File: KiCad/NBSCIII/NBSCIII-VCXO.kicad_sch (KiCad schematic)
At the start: 20 parts, among them Q1000 BC337-25, Q1001 2SC1906, X1000 6.000Mhz HC49/U

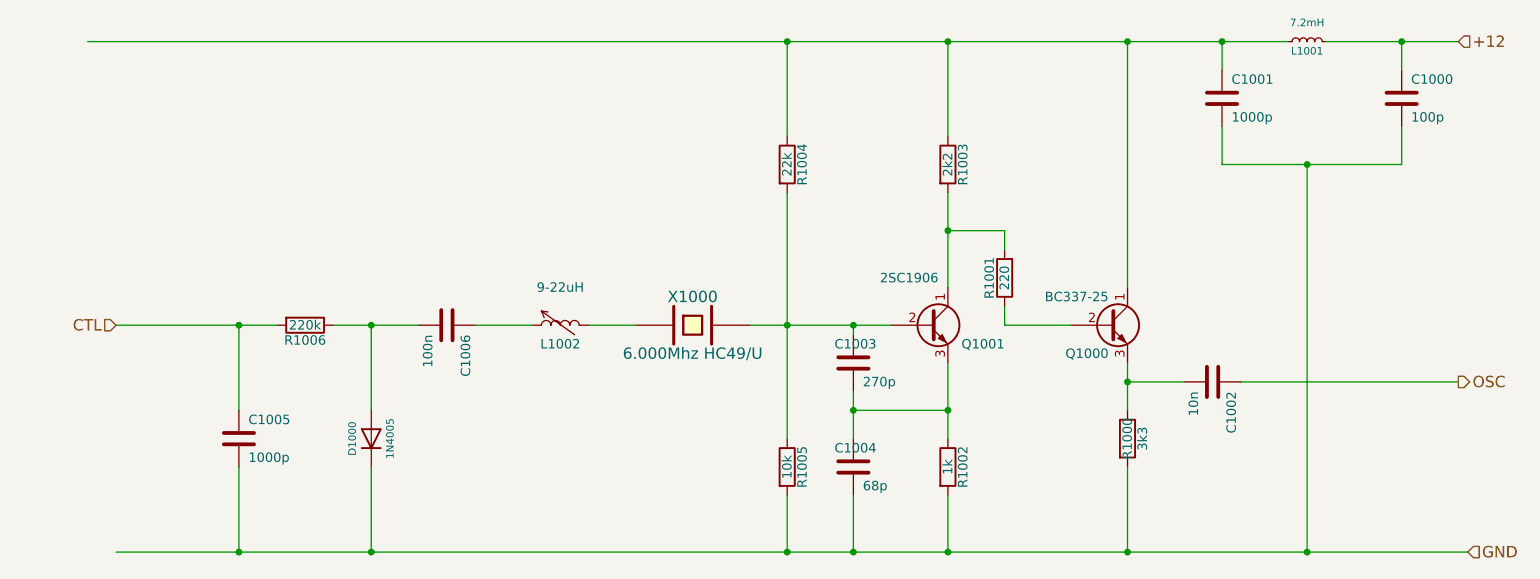
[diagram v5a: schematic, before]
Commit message: Simplify power distribution and make global
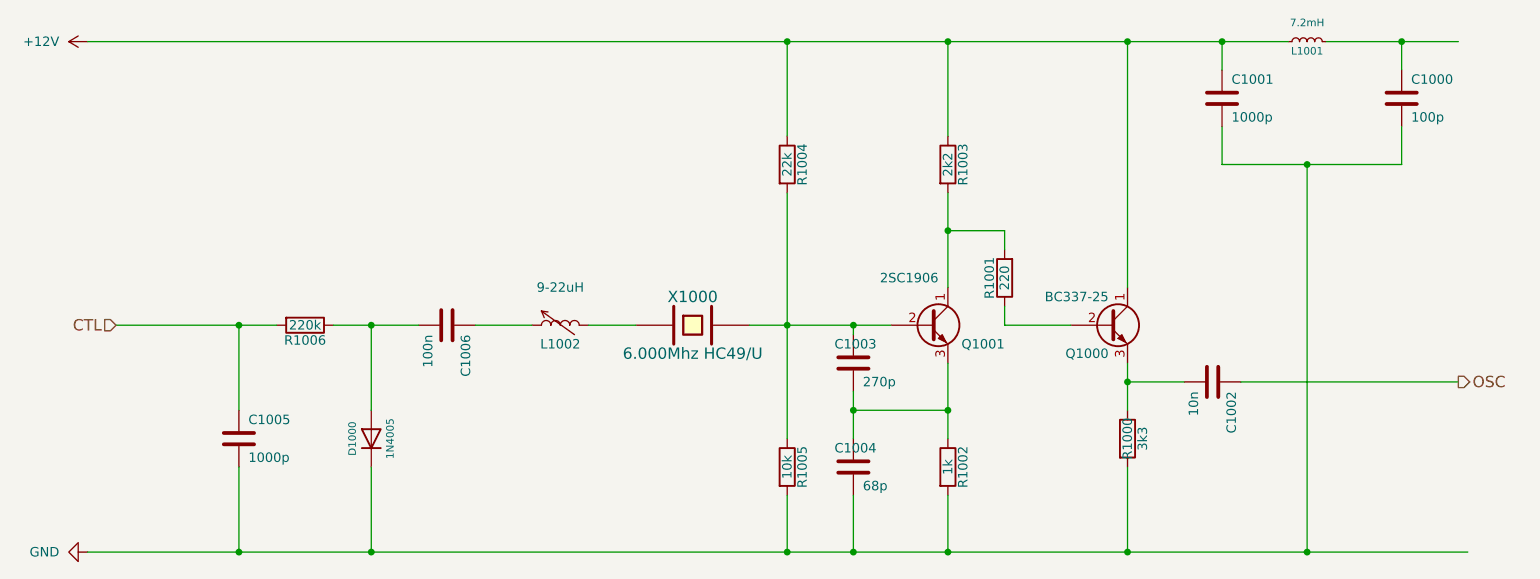
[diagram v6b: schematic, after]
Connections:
- net +12V: now reaches C1001.1, L1001.1, Q1000.1 (C), R1003.1, R1004.1
- net +12: no longer names the net of C1000.1, L1001.2
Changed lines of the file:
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@@
     (stroke (width 0) (type default) (color 0 0 0 0))
   )
-  (wire (pts (xy 46.99 123.19) (xy 63.5 123.19))
+  (wire (pts (xy 43.18 123.19) (xy 63.5 123.19))
     (stroke (width 0) (type default) (color 0 0 0 0))
   )
@@
   (wire (pts (xy 198.12 100.33) (xy 227.33 100.33))
     (stroke (width 0) (type default) (color 0 0 0 0))
-  )
-  (hierarchical_label "GND" (shape input) (at 228.6 123.19 0)
-    (effects (font (size 1.524 1.524)) (justify left))
   )
   (hierarchical_label "CTL" (shape input) (at 46.99 92.71 180)
@@
   )
   (hierarchical_label "OSC" (shape output) (at 227.33 100.33 0)
-    (effects (font (size 1.524 1.524)) (justify left))
-  )
-  (hierarchical_label "+12" (shape input) (at 227.33 54.61 0)
     (effects (font (size 1.524 1.524)) (justify left))
   )
@@
     (pin "2")
   )
+  (symbol (lib_id "power:GND") (at 43.18 123.19 270) (unit 1)
+    (in_bom yes) (on_board yes) (fields_autoplaced)
+    (property "Reference" "#PWR0129" (id 0) (at 36.83 123.19 0)
+      (effects (font (size 1.27 1.27)) hide)
+    )
+    (property "Value" "GND" (id 1) (at 39.37 123.1899 90)
+      (effects (font (size 1.27 1.27)) (justify right))
+    )
+    (property "Footprint" "" (id 2) (at 43.18 123.19 0)
+      (effects (font (size 1.27 1.27)) hide)
+    )
+    (property "Datasheet" "" (id 3) (at 43.18 123.19 0)
+      (effects (font (size 1.27 1.27)) hide)
+    )
+    (pin "1")
+  )
+  (symbol (lib_id "power:+12V") (at 43.18 54.61 90) (unit 1)
+    (in_bom yes) (on_board yes) (fields_autoplaced)
+    (property "Reference" "#PWR0128" (id 0) (at 46.99 54.61 0)
+      (effects (font (size 1.27 1.27)) hide)
+    )
+    (property "Value" "+12V" (id 1) (at 39.37 54.6099 90)
+      (effects (font (size 1.27 1.27)) (justify left))
+    )
+    (property "Footprint" "" (id 2) (at 43.18 54.61 0)
+      (effects (font (size 1.27 1.27)) hide)
+    )
+    (property "Datasheet" "" (id 3) (at 43.18 54.61 0)
+      (effects (font (size 1.27 1.27)) hide)
+    )
+    (pin "1")
+  )
 )

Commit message: unrescue crystal, Q1001 to NPN_BEC
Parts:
- Q1001: symbol Device:Q_NPN_CBE -> Device:Q_NPN_BEC
- X1000: symbol NBSCIII-rescue:CRYSTAL -> Device:Crystal
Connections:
- net at R1001.2, R1003.2: now also Q1001.3 (C); no longer Q1001.1 (C)
- net at C1003.1, R1004.2, R1005.1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: now also Q1001.1 (B); no longer Q1001.2 (B)
- net at C1003.2, C1004.1, R1002.1: now also Q1001.2 (E); no longer Q1001.3 (E)
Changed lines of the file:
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@@
     (stroke (width 0) (type default) (color 0 0 0 0))
   )
-  (wire (pts (xy 110.49 92.71) (xy 116.84 92.71))
+  (wire (pts (xy 110.49 92.71) (xy 120.65 92.71))
     (stroke (width 0) (type default) (color 0 0 0 0))
   )
@@
     (stroke (width 0) (type default) (color 0 0 0 0))
   )
-  (wire (pts (xy 137.16 92.71) (xy 132.08 92.71))
+  (wire (pts (xy 128.27 92.71) (xy 137.16 92.71))
     (stroke (width 0) (type default) (color 0 0 0 0))
   )
@@
     (pin "2")
   )
-  (symbol (lib_id "Device:Q_NPN_CBE") (at 156.21 92.71 0) (unit 1)
+  (symbol (lib_id "Device:Q_NPN_BEC") (at 156.21 92.71 0) (unit 1)
     (in_bom yes) (on_board yes)
     (property "Reference" "Q1001" (id 0) (at 166.37 95.25 0)
@@
       (effects (font (size 1.27 1.27)) (justify right))
     )
-    (property "Footprint" "" (id 2) (at 156.21 92.71 0)
-      (effects (font (size 1.27 1.27)) hide)
-    )
-    (property "Datasheet" "" (id 3) (at 156.21 92.71 0)
+    (property "Footprint" "" (id 2) (at 161.29 90.17 0)
+      (effects (font (size 1.27 1.27)) hide)
+    )
+    (property "Datasheet" "~" (id 3) (at 156.21 92.71 0)
       (effects (font (size 1.27 1.27)) hide)
     )
@@
     (pin "2")
   )
-  (symbol (lib_id "NBSCIII-rescue:CRYSTAL") (at 124.46 92.71 0) (unit 1)
+  (symbol (lib_id "Device:Crystal") (at 124.46 92.71 0) (unit 1)
     (in_bom yes) (on_board yes)
     (property "Reference" "X1000" (id 0) (at 124.46 88.9 0)
